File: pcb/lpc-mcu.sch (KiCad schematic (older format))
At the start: 10 parts, among them CON1 ARM-SWD-HEADER, IC1 LPC11U14FBD48, P4 GPIO, X1 CRYSTAL

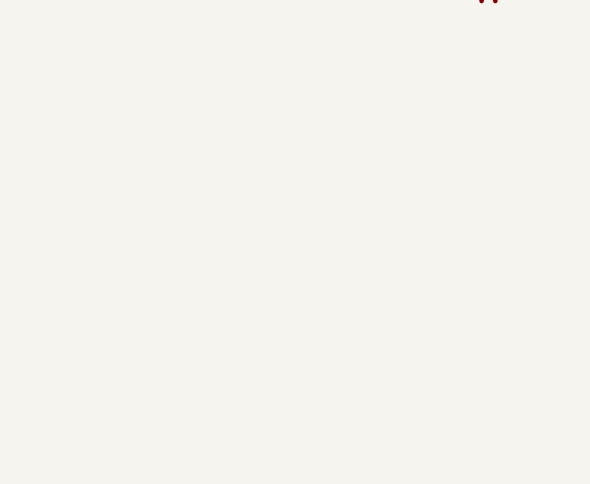
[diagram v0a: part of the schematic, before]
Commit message: added LED, and removed VLED from power sheet
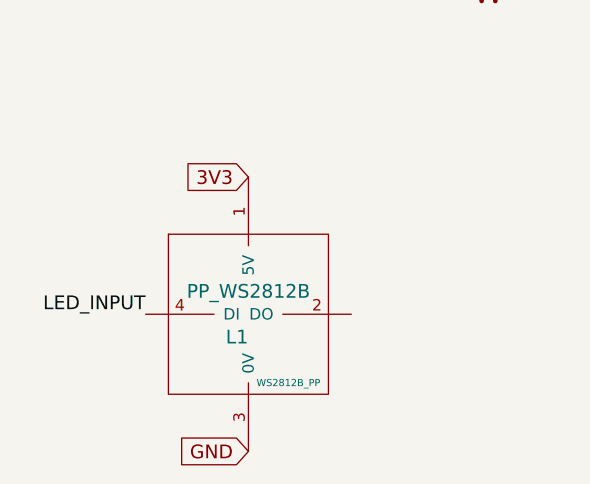
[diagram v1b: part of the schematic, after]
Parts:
- added L1: PP_WS2812B, WS2812B_PP, symbol PP_WS2812B
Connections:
- net 3V3: now also L1.1 (5V)
- net GND: now also L1.3 (0V)
- new net LED_INPUT: L1.4 (DI)
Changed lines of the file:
@@
 	1    0    0    -1
 $EndComp
+$Comp
+L PP_WS2812B L1
+U 1 1 549E8468
+P 2050 7100
+F 0 "L1" H 2000 7350 60  0000 C CNN
+F 1 "PP_WS2812B" H 2050 7550 60  0000 C CNN
+F 2 "WS2812B_PP" H 2225 7150 31  0000 C CNN
+F 3 "~" H 2050 7100 60  0000 C CNN
+	1    2050 7100
+	1    0    0    -1
+$EndComp
+Text GLabel 2050 6150 0    60   Input ~ 0
+3V3
+Text GLabel 2050 7350 0    60   Input ~ 0
+GND
+Text Label 1600 6750 2    60   ~ 0
+LED_INPUT
 $EndSCHEMATC

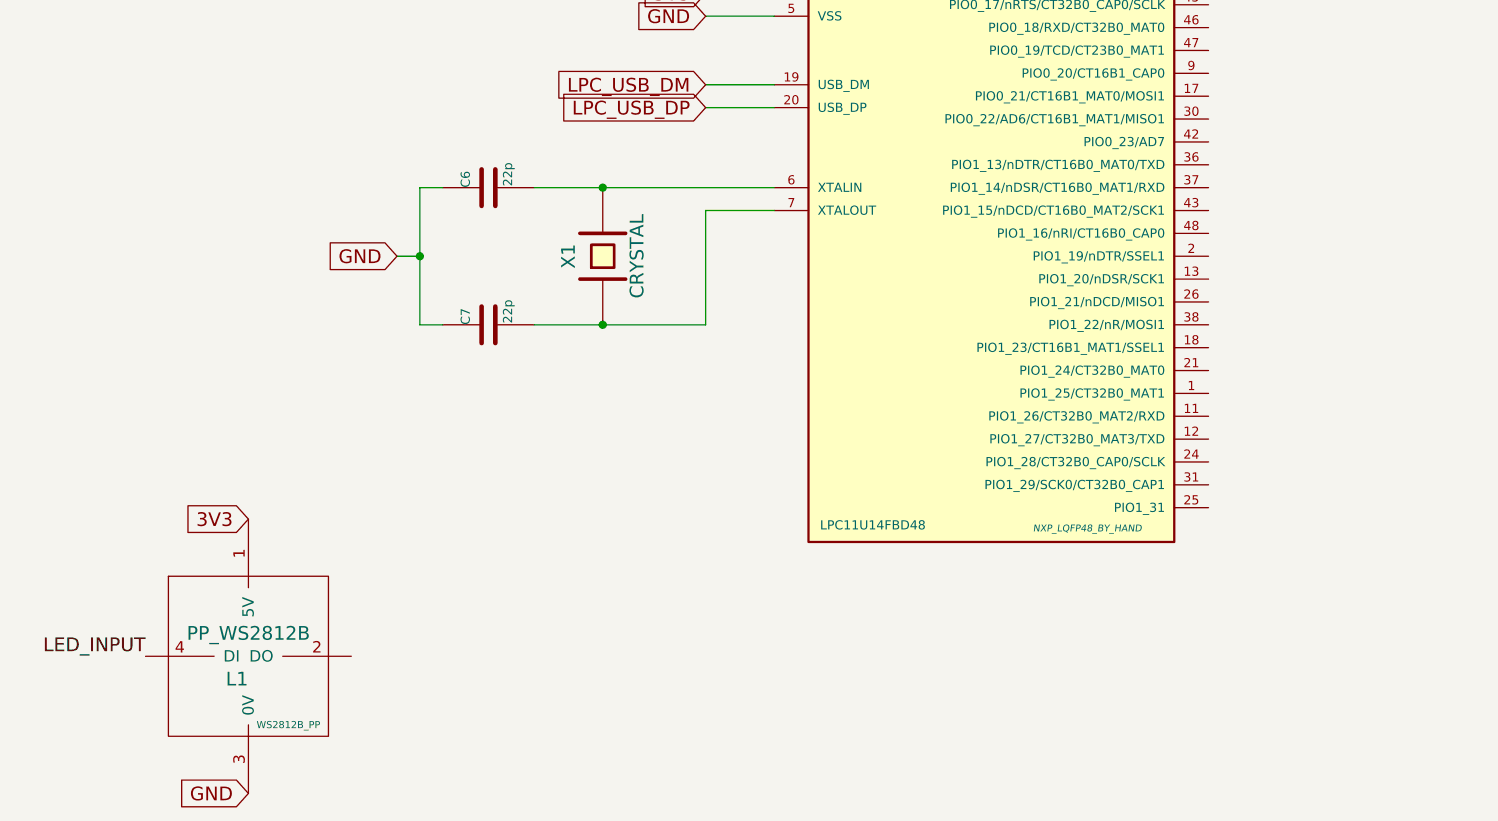
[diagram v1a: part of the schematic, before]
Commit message: some labels, and changed sm0805 parts to use my nosilkscreen package
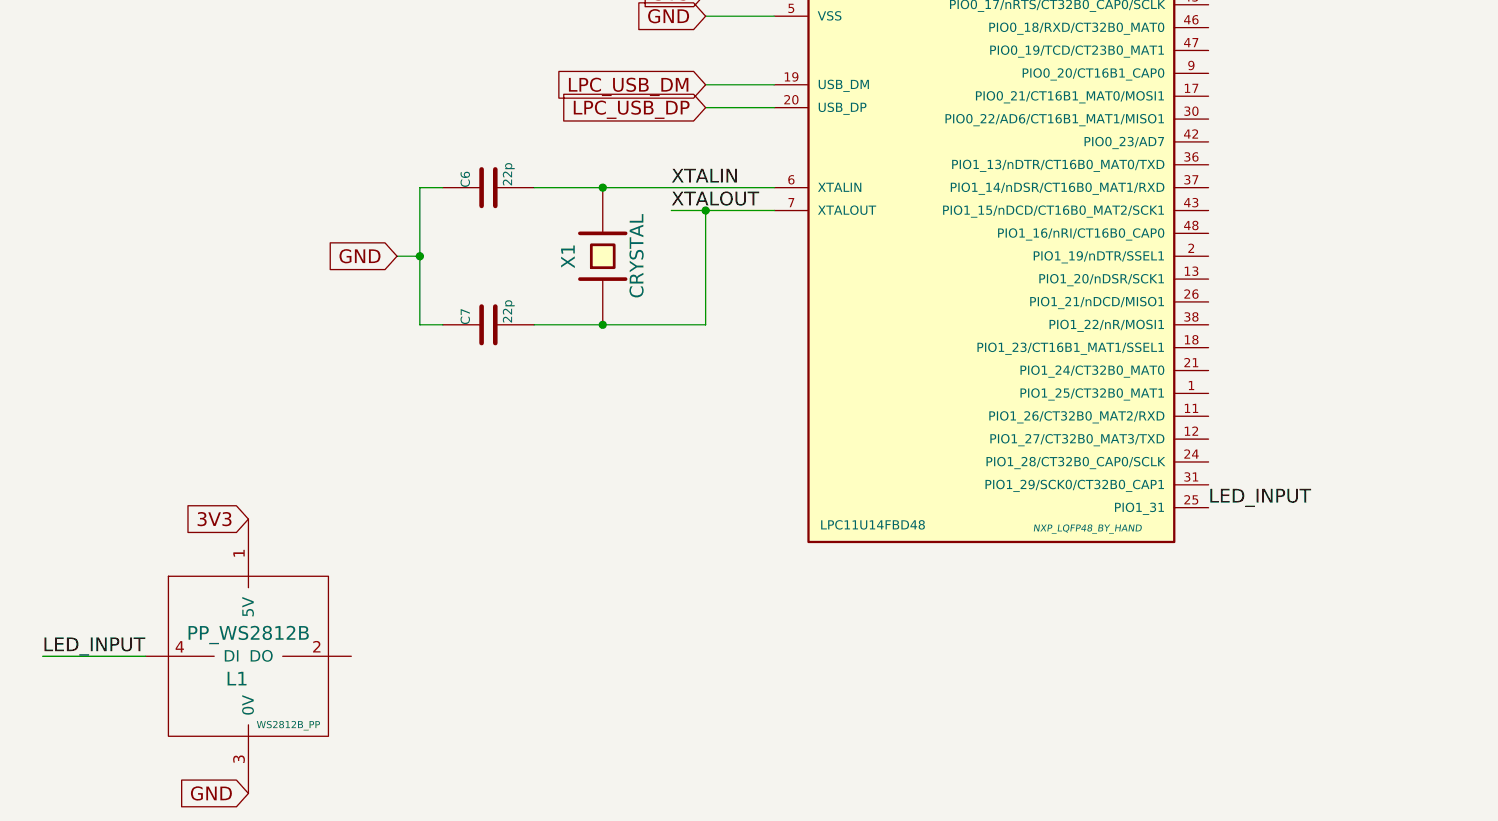
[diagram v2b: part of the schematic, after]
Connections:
- net LED_INPUT: now also IC1.25 (PIO1_31)
- net XTALIN: now reaches C6.2, IC1.6 (XTALIN), X1.2
- net XTALOUT: now reaches C7.2, IC1.7 (XTALOUT), X1.1
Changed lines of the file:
@@
 	4050 5300 4050 4800
 Wire Wire Line
-	4050 4800 4350 4800
+	3900 4800 4350 4800
 Connection ~ 3600 5300
 $Comp
@@
 Text GLabel 2050 7350 0    60   Input ~ 0
 GND
-Text Label 1600 6750 2    60   ~ 0
+Text Label 1150 6750 0    60   ~ 0
+LED_INPUT
+Text Label 3900 4700 0    60   ~ 0
+XTALIN
+Text Label 3900 4800 0    60   ~ 0
+XTALOUT
+Connection ~ 4050 4800
+Wire Wire Line
+	1150 6750 1600 6750
+Text Label 6250 6100 0    60   ~ 0
 LED_INPUT
 $EndSCHEMATC

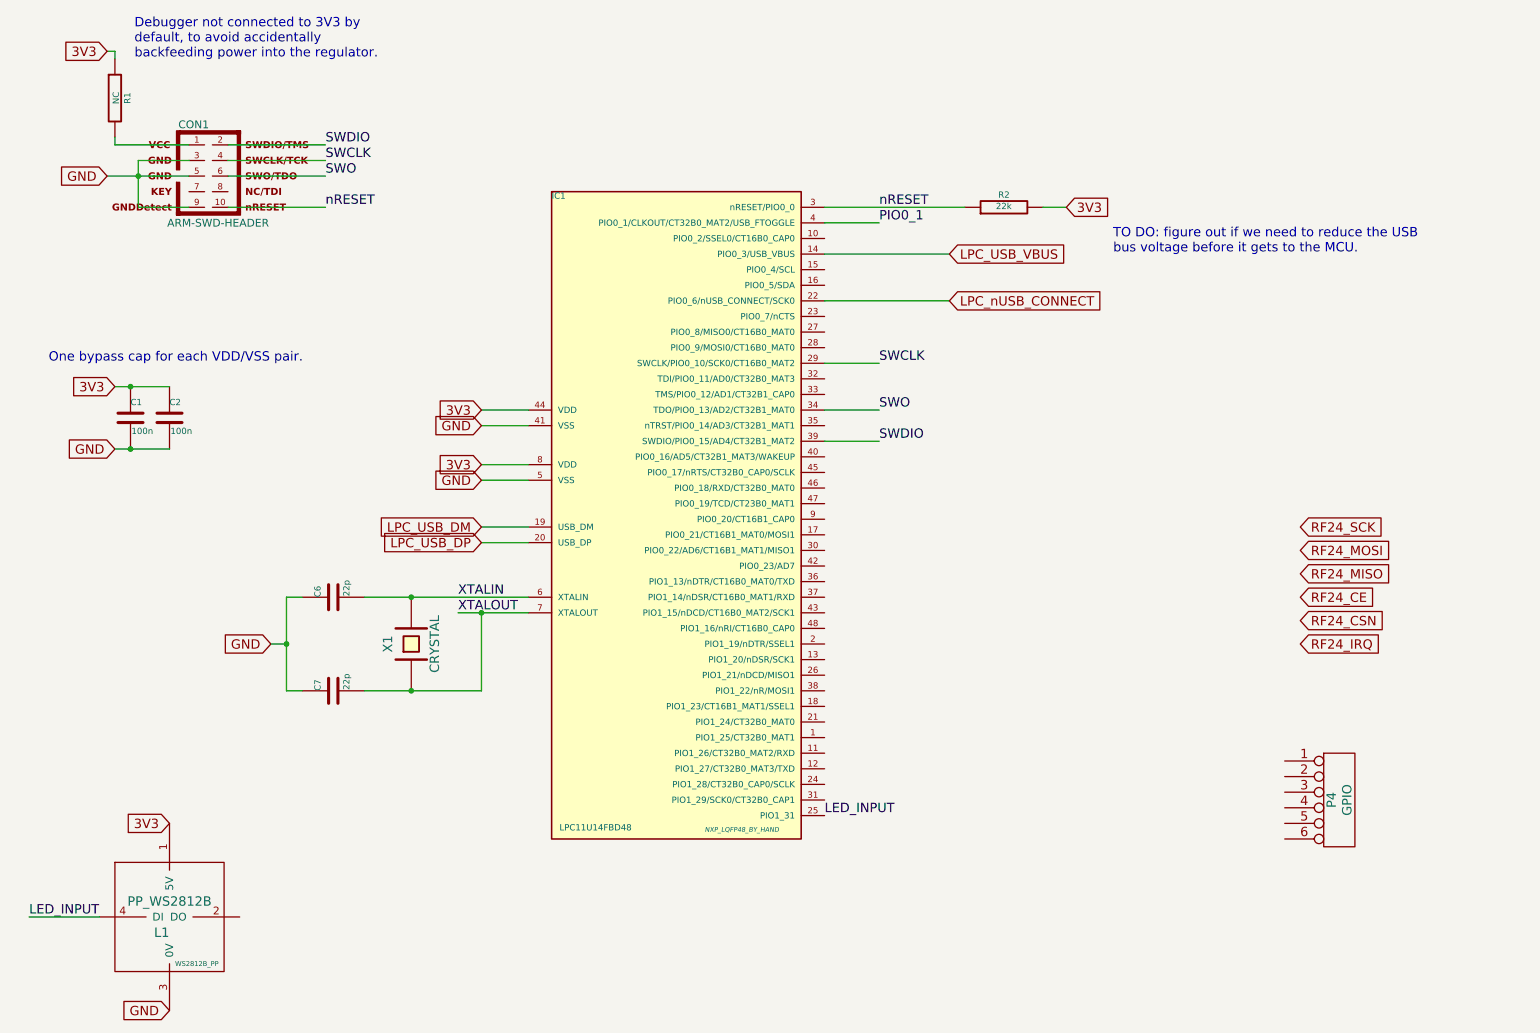
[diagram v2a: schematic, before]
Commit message: gpios and rf24 connections
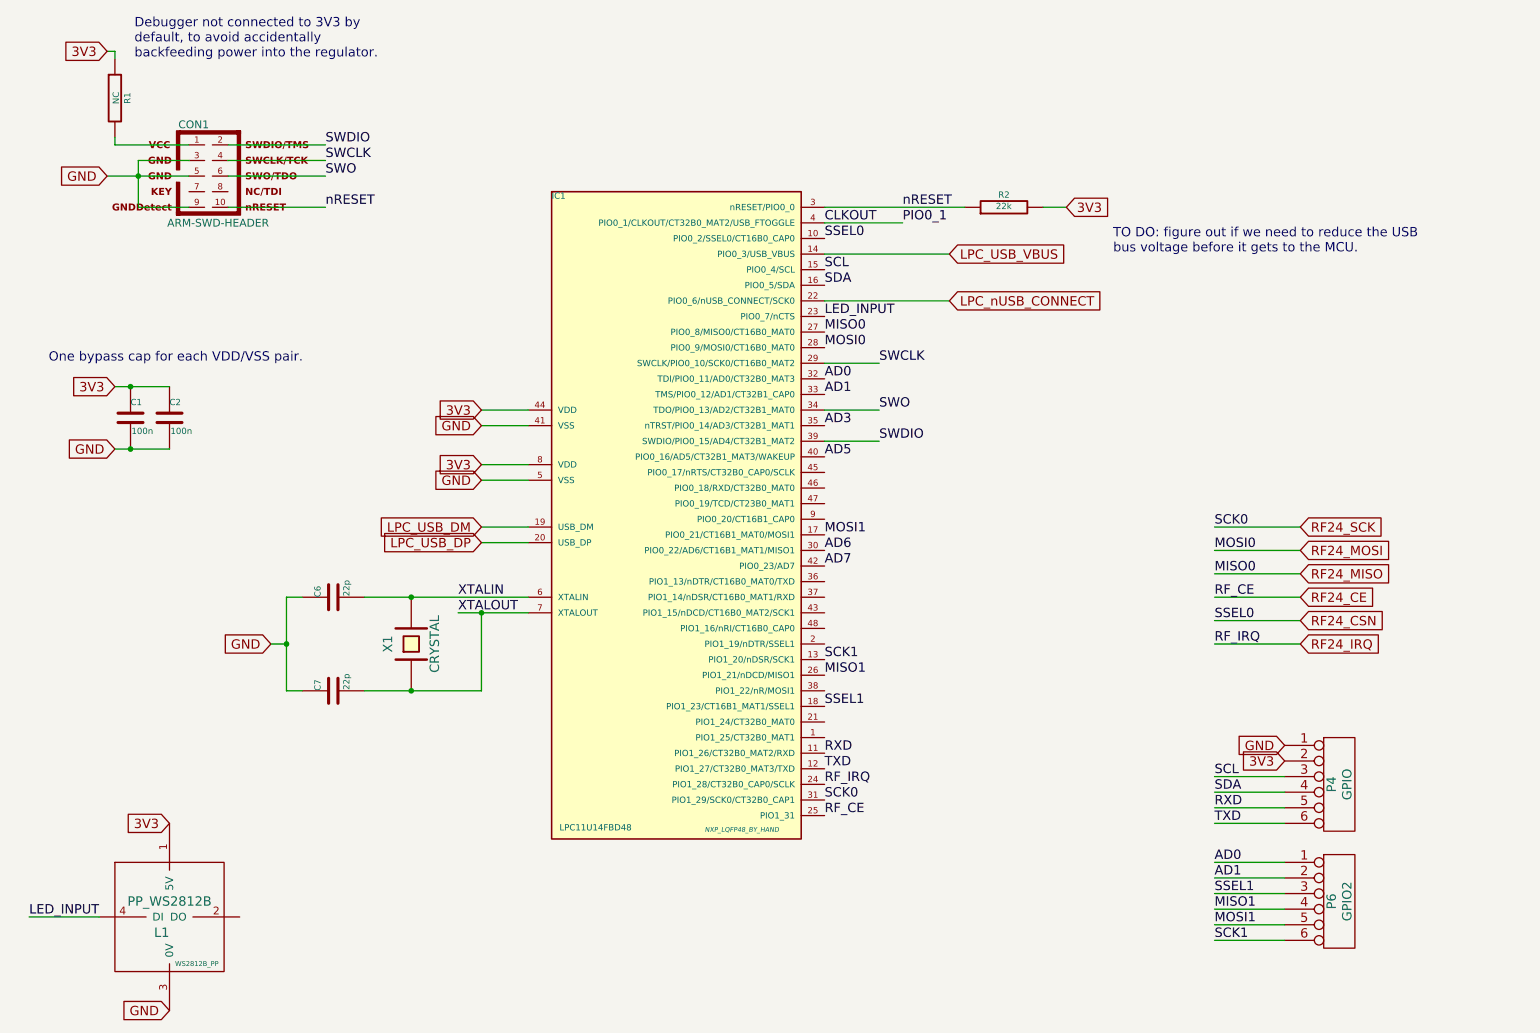
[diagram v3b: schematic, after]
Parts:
- added P6: GPIO2, symbol CONN_6
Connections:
- net 3V3: now also P4.2
- net GND: now also P4.1
- net LED_INPUT: now also IC1.23 (PIO0_7/nCTS); no longer IC1.25 (PIO1_31)
- net RF24_CE: now also IC1.25 (PIO1_31)
- net RF24_CSN: now also IC1.10 (PIO0_2/SSEL0/CT16B0_CAP0)
- net RF24_IRQ: now also IC1.24 (PIO1_28/CT32B0_CAP0/SCLK)
- net RF24_MISO: now also IC1.27 (PIO0_8/MISO0/CT16B0_MAT0)
- net RF24_MOSI: now also IC1.28 (PIO0_9/MOSI0/CT16B0_MAT0)
- net RF24_SCK: now also IC1.31 (PIO1_29/SCK0/CT32B0_CAP1)
- net RXD: now reaches IC1.11 (PIO1_26/CT32B0_MAT2/RXD)
- net RXD: now also P4.5
- net TXD: now reaches IC1.12 (PIO1_27/CT32B0_MAT3/TXD)
- net TXD: now also P4.6
- net SCK1: now reaches IC1.13 (PIO1_20/nDSR/SCK1)
- net SCK1: now also P6.6
- net SCL: now reaches IC1.15 (PIO0_4/SCL)
- net SCL: now also P4.3
- net SDA: now reaches IC1.16 (PIO0_5/SDA)
- net SDA: now also P4.4
- net MOSI1: now reaches IC1.17 (PIO0_21/CT16B1_MAT0/MOSI1)
- net MOSI1: now also P6.5
- net SSEL1: now reaches IC1.18 (PIO1_23/CT16B1_MAT1/SSEL1)
- net SSEL1: now also P6.3
- net MISO1: now reaches IC1.26 (PIO1_21/nDCD/MISO1)
- net MISO1: now also P6.4
- net AD6: now reaches IC1.30 (PIO0_22/AD6/CT16B1_MAT1/MISO1)
- net AD0: now reaches IC1.32 (TDI/PIO0_11/AD0/CT32B0_MAT3)
- net AD0: now also P6.1
- net AD1: now reaches IC1.33 (TMS/PIO0_12/AD1/CT32B1_CAP0)
- net AD1: now also P6.2
- net AD3: now reaches IC1.35 (nTRST/PIO0_14/AD3/CT32B1_MAT1)
- net AD5: now reaches IC1.40 (PIO0_16/AD5/CT32B1_MAT3/WAKEUP)
- net AD7: now reaches IC1.42 (PIO0_23/AD7)
- net PIO0_1 renamed CLKOUT
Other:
- moved on the sheet: P4
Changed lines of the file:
@@
 Text GLabel 4050 4350 0    60   Input ~ 0
 LPC_USB_DP
-Text Label 6600 2200 0    60   ~ 0
+Text Label 6750 2200 0    60   ~ 0
 nRESET
 Text GLabel 7050 2500 2    60   Input ~ 0
 LPC_USB_VBUS
-Text Label 6600 2300 0    60   ~ 0
+Text Label 6750 2300 0    60   ~ 0
 PIO0_1
 Wire Wire Line
-	6600 2300 6250 2300
+	6250 2300 6750 2300
 Wire Wire Line
 	7050 2500 6250 2500
@@
 L CONN_6 P4
 U 1 1 549E7D82
-P 9550 6000
-F 0 "P4" V 9500 6000 60  0000 C CNN
-F 1 "GPIO" V 9600 6000 60  0000 C CNN
-F 2 "" H 9550 6000 60  0000 C CNN
-F 3 "" H 9550 6000 60  0000 C CNN
-	1    9550 6000
+P 9550 5900
+F 0 "P4" V 9500 5900 60  0000 C CNN
+F 1 "GPIO" V 9600 5900 60  0000 C CNN
+F 2 "" H 9550 5900 60  0000 C CNN
+F 3 "" H 9550 5900 60  0000 C CNN
+	1    9550 5900
 	1    0    0    -1
 $EndComp
@@
 Wire Wire Line
 	1150 6750 1600 6750
+Text Label 6250 2900 0    60   ~ 0
+LED_INPUT
+Text Label 6250 2600 0    60   ~ 0
+SCL
+Text Label 6250 2700 0    60   ~ 0
+SDA
+Text GLabel 9200 5650 0    60   Input ~ 0
+GND
+Text Label 8750 5850 0    60   ~ 0
+SCL
+Text Label 8750 5950 0    60   ~ 0
+SDA
+Wire Wire Line
+	8750 5950 9200 5950
+Wire Wire Line
+	9200 5850 8750 5850
+Text Label 6250 6000 0    60   ~ 0
+SCK0
+Text Label 6250 3100 0    60   ~ 0
+MOSI0
+Text Label 6250 3000 0    60   ~ 0
+MISO0
+Text Label 6250 2400 0    60   ~ 0
+SSEL0
+Text Label 6250 5100 0    60   ~ 0
+SCK1
+Text Label 6250 4300 0    60   ~ 0
+MOSI1
+Text Label 6250 5200 0    60   ~ 0
+MISO1
+Text Label 6250 5400 0    60   ~ 0
+SSEL1
+Text Label 6250 3300 0    60   ~ 0
+AD0
+Text Label 6250 3400 0    60   ~ 0
+AD1
+Text Label 6250 3600 0    60   ~ 0
+AD3
+Text Label 6250 3800 0    60   ~ 0
+AD5
+Text Label 6250 4400 0    60   ~ 0
+AD6
+Text Label 6250 4500 0    60   ~ 0
+AD7
+Text Label 6250 2300 0    60   ~ 0
+CLKOUT
+Text Label 6250 5700 0    60   ~ 0
+RXD
+Text Label 6250 5800 0    60   ~ 0
+TXD
+Text Label 8750 6050 0    60   ~ 0
+RXD
+Text Label 8750 6150 0    60   ~ 0
+TXD
+Wire Wire Line
+	8750 6050 9200 6050
+Wire Wire Line
+	9200 6150 8750 6150
+Text Label 8750 4250 0    60   ~ 0
+SCK0
+Text Label 8750 4400 0    60   ~ 0
+MOSI0
+Text Label 8750 4550 0    60   ~ 0
+MISO0
+Text Label 8750 4850 0    60   ~ 0
+SSEL0
+Wire Wire Line
+	8750 4850 9300 4850
+Wire Wire Line
+	9300 4550 8750 4550
+Wire Wire Line
+	8750 4400 9300 4400
+Wire Wire Line
+	9300 4250 8750 4250
+Wire Wire Line
+	8750 4700 9300 4700
+Wire Wire Line
+	8750 5000 9300 5000
 Text Label 6250 6100 0    60   ~ 0
-LED_INPUT
+RF_CE
+Text Label 8750 4700 0    60   ~ 0
+RF_CE
+Text Label 8750 5000 0    60   ~ 0
+RF_IRQ
+Text Label 6250 5900 0    60   ~ 0
+RF_IRQ
+Text GLabel 9200 5750 0    60   Input ~ 0
+3V3
+$Comp
+L CONN_6 P6
+U 1 1 549E9A45
+P 9550 6650
+F 0 "P6" V 9500 6650 60  0000 C CNN
+F 1 "GPIO2" V 9600 6650 60  0000 C CNN
+F 2 "" H 9550 6650 60  0000 C CNN
+F 3 "" H 9550 6650 60  0000 C CNN
+	1    9550 6650
+	1    0    0    -1
+$EndComp
+Wire Wire Line
+	8750 6400 9200 6400
+Wire Wire Line
+	8750 6500 9200 6500
+Wire Wire Line
+	8750 6600 9200 6600
+Wire Wire Line
+	8750 6700 9200 6700
+Wire Wire Line
+	8750 6800 9200 6800
+Wire Wire Line
+	8750 6900 9200 6900
+Text Label 8750 6400 0    60   ~ 0
+AD0
+Text Label 8750 6500 0    60   ~ 0
+AD1
+Text Label 8750 6900 0    60   ~ 0
+SCK1
+Text Label 8750 6800 0    60   ~ 0
+MOSI1
+Text Label 8750 6700 0    60   ~ 0
+MISO1
+Text Label 8750 6600 0    60   ~ 0
+SSEL1
 $EndSCHEMATC
